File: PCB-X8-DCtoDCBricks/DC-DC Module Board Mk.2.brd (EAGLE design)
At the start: 177.8 x 102.9 mm, 151 parts, among them T1 FDN340P, T2 AP1117_LIN_REG, U3 LM1085IS-5.0

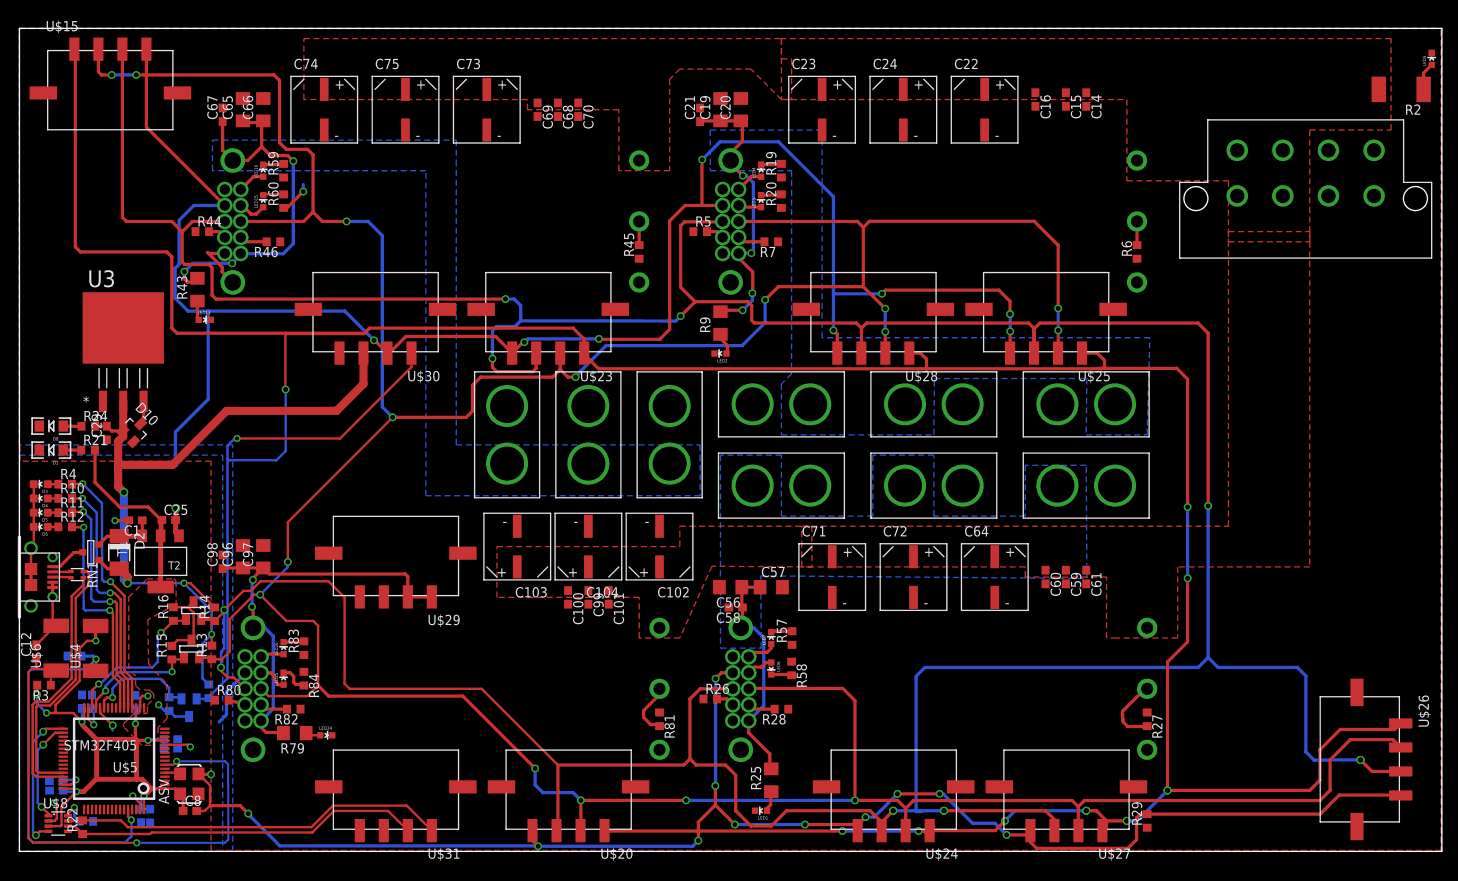
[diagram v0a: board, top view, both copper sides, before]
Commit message: top GND plane and clean up
Added top ground plane, cleaned up messy signals and other mistakes
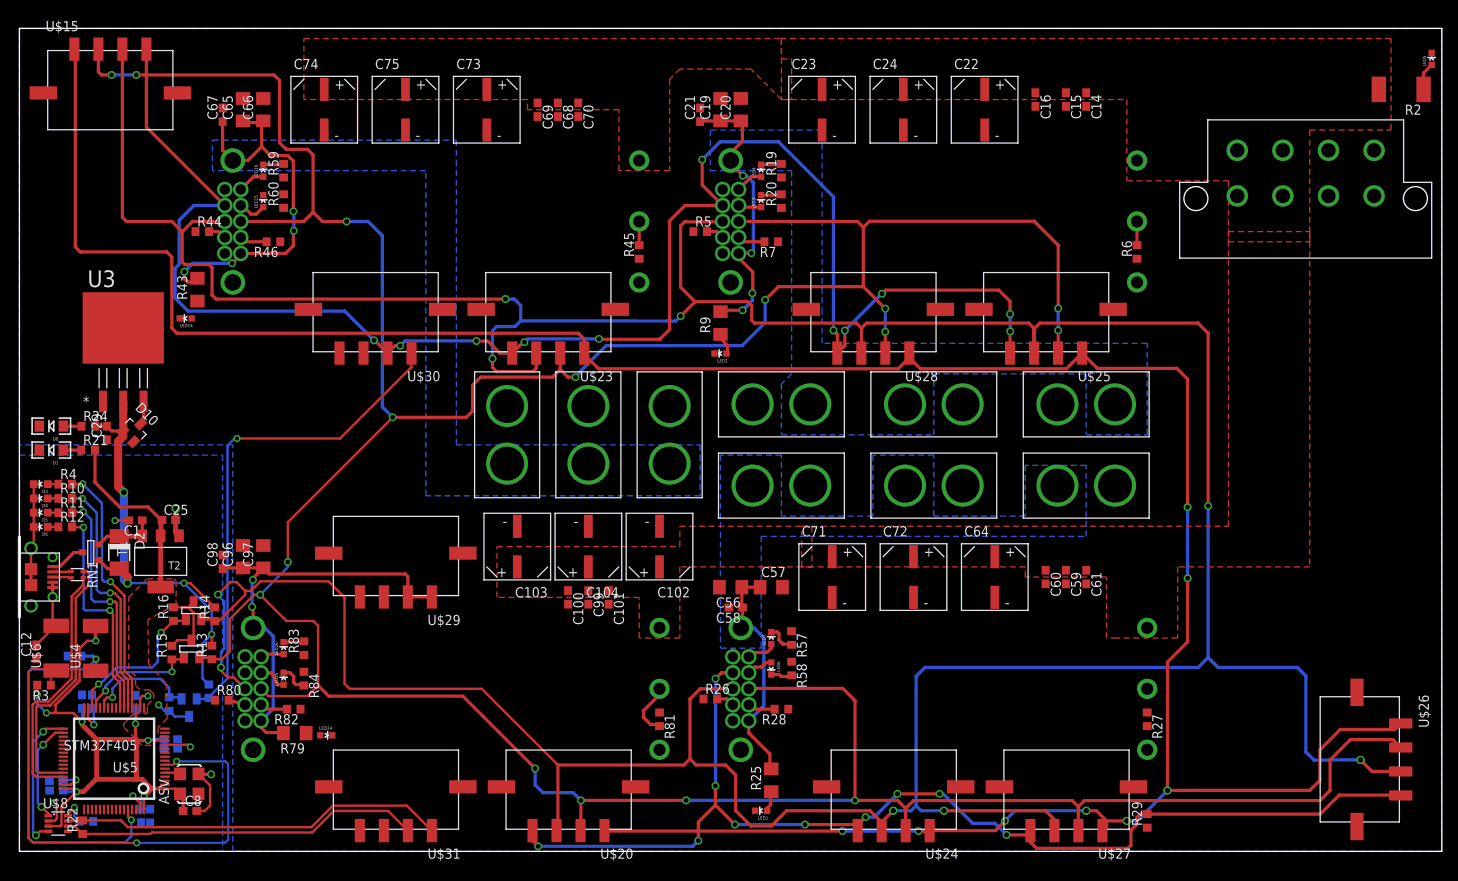
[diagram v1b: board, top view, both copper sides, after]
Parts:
- moved LED14 2.39 mm to (20.8, 65.4), turned to 90 degrees
- moved R57 0.05 mm to (96.5, 25.4), turned to 270 degrees
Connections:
- new net PWM: U$15.C4, U$20.C4, U$23.C4, U$24.C4, U$25.C4, U$26.C4, U$27.C4, U$28.C4
- net DGND: no longer U$5.28
- net GND: now also U$5.28
- net PWM_OUT: no longer U$15.C4, U$20.C4, U$23.C4, U$24.C4, U$25.C4, U$26.C4, U$27.C4, U$28.C4
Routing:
- net PWM_OUT: track 446.2 -> 63.0 mm, vias 10 -> 1
- net PWM: track 0.00 -> 344.2 mm, vias 0 -> 8
- net DGND: track 468.8 -> 397.9 mm, vias 27 -> 28
- net +5V: track 99.8 -> 61.0 mm
- net GND: track 11.3 -> 0.00 mm, vias 1 -> 0
- net N$8: track 8.87 -> 0.00 mm
- net SDA: track 520.4 -> 526.8 mm
- net N$36: track 2.58 -> 0.00 mm
- net N$23: track 2.41 -> 0.00 mm
- net N$43: track 1.88 -> 0.00 mm
- net NRST: track 70.8 -> 69.5 mm
- net N$33: track 2.69 -> 3.69 mm
- net +12V2: track 48.6 -> 48.7 mm, vias 3 -> 4
- removed copper zone on layer 1, net GND
